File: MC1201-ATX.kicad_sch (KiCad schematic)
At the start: 248 parts, among them J1 PLD-16, J2 PLD-16, J3 PLD-16, J4 ATX-20, J5 Conn_01x01_Pin, J6 Conn_01x01_Pin, J7 Conn_01x09_Pin, P1 Conn_01x01_Pin, P10 Conn_01x01_Pin, P11 Conn_01x01_Pin, P12 Conn_01x01_Pin, P13 Conn_01x01_Pin, P14 Conn_01x01_Pin, P15 Conn_01x01_Pin, P16 Conn_01x01_Pin, P17 Conn_01x01_Pin, P18 Conn_01x01_Pin, P2 Conn_01x01_Pin, P3 Conn_01x01_Pin, P4 Conn_01x01_Pin, P5 Conn_01x01_Pin, P6 Conn_01x01_Pin, P7 Conn_01x01_Pin, P8 Conn_01x01_Pin, P9 Conn_01x01_Pin, Q1 BC547, X2 AFPC, X3 QBUS_DWK_64Pin_MBT

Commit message: Some notes, proper signal names
/MMIO renamed to /HIGHMEM, added some more net names for future references
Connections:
- net CPU_DIN: now reaches DD10.10, DD10.9, DD11.1 (CA), DD12.1 (CA), DD13.1 (CA), DD14.1 (CA), DD19.1, DD6.11, DD6.2, R3.1
- net LOCK: now reaches DD5.5, DD9.9
- net ~{MMIO} renamed ~{HIGHMEM}
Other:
- note added: "ERRATUM E0005 Сигнал LOCK не реализован."
- note removed: "ERRATUM E0005 Не подключенные входы."
- moved on the sheet: E10_5, E11_1
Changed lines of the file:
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@@
 		)
 	)
-	(text "ERRATUM E0005\nНе подключенные входы."
+	(text "ERRATUM E0005\nСигнал LOCK не реализован."
 		(exclude_from_sim no)
-		(at 154.178 238.506 0)
+		(at 149.098 237.744 0)
 		(effects
 			(font
@@
 	)
 	(junction
+		(at 568.96 207.01)
+		(diameter 0)
+		(color 0 0 0 0)
+	)
+	(junction
 		(at 29.21 398.78)
 		(diameter 0)
@@
 	)
 	(junction
-		(at 566.42 207.01)
-		(diameter 0)
-		(color 0 0 0 0)
-	)
-	(junction
 		(at 320.1029 182.88)
 		(diameter 0)
@@
 	)
 	(junction
+		(at 163.83 241.3)
+		(diameter 0)
+		(color 0 0 0 0)
+	)
+	(junction
 		(at 194.31 59.69)
 		(diameter 0)
@@
 	)
 	(junction
-		(at 568.96 196.85)
-		(diameter 0)
-		(color 0 0 0 0)
-	)
-	(junction
 		(at 146.05 156.21)
 		(diameter 0)
@@
 	)
 	(junction
-		(at 566.42 125.73)
-		(diameter 0)
-		(color 0 0 0 0)
-	)
-	(junction
 		(at 528.32 224.79)
 		(diameter 0)
@@
 	)
 	(junction
+		(at 572.77 196.85)
+		(diameter 0)
+		(color 0 0 0 0)
+	)
+	(junction
 		(at 382.27 41.91)
 		(diameter 0)
@@
 	)
 	(junction
+		(at 568.96 125.73)
+		(diameter 0)
+		(color 0 0 0 0)
+	)
+	(junction
 		(at 314.96 383.54)
 		(diameter 0)
@@
 	(wire
 		(pts
+			(xy 568.96 123.19) (xy 568.96 125.73)
+		)
+		(stroke
+			(width 0)
+			(type default)
+		)
+	)
+	(wire
+		(pts
 			(xy 283.21 109.22) (xy 288.29 109.22)
 		)
@@
 	(wire
 		(pts
+			(xy 161.29 241.3) (xy 163.83 241.3)
+		)
+		(stroke
+			(width 0)
+			(type default)
+			(color 255 0 0 1)
+		)
+	)
+	(wire
+		(pts
 			(xy 283.21 39.37) (xy 288.29 39.37)
 		)
@@
 	(wire
 		(pts
+			(xy 558.8 125.73) (xy 568.96 125.73)
+		)
+		(stroke
+			(width 0)
+			(type default)
+		)
+	)
+	(wire
+		(pts
 			(xy 481.33 347.98) (xy 499.11 347.98)
 		)
@@
 	(wire
 		(pts
-			(xy 430.53 247.65) (xy 568.96 247.65)
+			(xy 430.53 247.65) (xy 572.77 247.65)
 		)
 		(stroke
@@
 	(wire
 		(pts
-			(xy 368.3 245.11) (xy 566.42 245.11)
+			(xy 368.3 245.11) (xy 568.96 245.11)
 		)
 		(stroke
@@
 	(wire
 		(pts
-			(xy 566.42 125.73) (xy 558.8 125.73)
-		)
-		(stroke
-			(width 0)
-			(type default)
-		)
-	)
-	(wire
-		(pts
-			(xy 541.02 207.01) (xy 566.42 207.01)
+			(xy 541.02 207.01) (xy 568.96 207.01)
 		)
 		(stroke
@@
 	(wire
 		(pts
-			(xy 566.42 245.11) (xy 566.42 207.01)
+			(xy 568.96 245.11) (xy 568.96 207.01)
 		)
 		(stroke
@@
 	(wire
 		(pts
-			(xy 568.96 196.85) (xy 541.02 196.85)
+			(xy 541.02 196.85) (xy 572.77 196.85)
 		)
 		(stroke
@@
 	(wire
 		(pts
-			(xy 568.96 247.65) (xy 568.96 196.85)
+			(xy 572.77 247.65) (xy 572.77 196.85)
 		)
 		(stroke
@@
 	(wire
 		(pts
-			(xy 566.42 207.01) (xy 566.42 125.73)
+			(xy 568.96 207.01) (xy 568.96 125.73)
 		)
 		(stroke
@@
 		)
 	)
+	(label "CPU_DIN"
+		(at 392.43 228.6 0)
+		(effects
+			(font
+				(size 1.27 1.27)
+			)
+			(justify left bottom)
+		)
+	)
 	(label "~{AD15}"
 		(at 377.19 208.28 0)
@@
 		)
 	)
-	(label "~{MMIO}"
-		(at 560.07 125.73 0)
+	(label "~{HIGHMEM}"
+		(at 558.8 125.73 0)
 		(effects
 			(font
@@
 		)
 	)
+	(global_label "LOCK"
+		(shape input)
+		(at 161.29 241.3 180)
+		(fields_autoplaced yes)
+		(effects
+			(font
+				(size 1.27 1.27)
+			)
+			(justify right)
+		)
+		(property "Intersheetrefs" "${INTERSHEET_REFS}"
+			(at 153.4062 241.3 0)
+			(hide yes)
+			(show_name no)
+			(do_not_autoplace no)
+			(effects
+				(font
+					(size 1.27 1.27)
+				)
+				(justify right)
+			)
+		)
+	)
 	(global_label "~{IRQ3}"
 		(shape input)
@@
 	(symbol
 		(lib_id "Device:R")
-		(at 568.96 193.04 0)
+		(at 572.77 193.04 0)
 		(unit 1)
 		(body_style 1)
@@
 		(dnp no)
 		(property "Reference" "E10_5"
-			(at 569.214 196.85 0)
+			(at 573.024 196.85 0)
 			(show_name no)
 			(do_not_autoplace no)
@@
 		)
 		(property "Value" "2.2K"
-			(at 569.468 198.882 0)
+			(at 573.278 198.882 0)
 			(show_name no)
 			(do_not_autoplace no)
@@
 		)
 		(property "Footprint" "Resistor_THT:R_Axial_DIN0204_L3.6mm_D1.6mm_P7.62mm_Horizontal"
-			(at 567.182 193.04 90)
+			(at 570.992 193.04 90)
 			(hide yes)
 			(show_name no)
@@
 		)
 		(property "Datasheet" ""
-			(at 568.96 193.04 0)
+			(at 572.77 193.04 0)
 			(hide yes)
 			(show_name no)
@@
 		)
 		(property "Description" "Resistor"
-			(at 568.96 193.04 0)
+			(at 572.77 193.04 0)
 			(hide yes)
 			(show_name no)
@@
 	(symbol
 		(lib_id "Device:R")
-		(at 566.42 121.92 0)
+		(at 568.96 119.38 0)
 		(unit 1)
 		(body_style 1)
@@
 		(fields_autoplaced yes)
 		(property "Reference" "E11_1"
-			(at 568.96 120.6499 0)
+			(at 571.5 118.1099 0)
 			(show_name no)
 			(do_not_autoplace no)
@@
 		)
 		(property "Value" "2.2K"
-			(at 568.96 123.1899 0)
+			(at 571.5 120.6499 0)
 			(show_name no)
 			(do_not_autoplace no)
@@
 		)
 		(property "Footprint" "Resistor_THT:R_Axial_DIN0204_L3.6mm_D1.6mm_P7.62mm_Horizontal"
-			(at 564.642 121.92 90)
+			(at 567.182 119.38 90)
 			(hide yes)
 			(show_name no)
@@
 		)
 		(property "Datasheet" ""
-			(at 566.42 121.92 0)
+			(at 568.96 119.38 0)
 			(hide yes)
 			(show_name no)
@@
 		)
 		(property "Description" "Resistor"
-			(at 566.42 121.92 0)
+			(at 568.96 119.38 0)
 			(hide yes)
 			(show_name no)
@@
 	(symbol
 		(lib_id "power:VCC")
-		(at 568.96 189.23 0)
+		(at 572.77 189.23 0)
 		(unit 1)
 		(body_style 1)
@@
 		(fields_autoplaced yes)
 		(property "Reference" "#PWR066"
-			(at 568.96 193.04 0)
+			(at 572.77 193.04 0)
 			(hide yes)
 			(show_name no)
@@
 		)
 		(property "Value" "VCC"
-			(at 568.96 184.15 0)
+			(at 572.77 184.15 0)
 			(show_name no)
 			(do_not_autoplace no)
@@
 		)
 		(property "Footprint" ""
-			(at 568.96 189.23 0)
+			(at 572.77 189.23 0)
 			(hide yes)
 			(show_name no)
@@
 		)
 		(property "Datasheet" ""
-			(at 568.96 189.23 0)
+			(at 572.77 189.23 0)
 			(hide yes)
 			(show_name no)
@@
 		)
 		(property "Description" "Power symbol creates a global label with name \"VCC\""
-			(at 568.96 189.23 0)
+			(at 572.77 189.23 0)
 			(hide yes)
 			(show_name no)
@@
 	(symbol
 		(lib_id "power:VCC")
-		(at 566.42 118.11 0)
+		(at 568.96 115.57 0)
 		(unit 1)
 		(body_style 1)
@@
 		(fields_autoplaced yes)
 		(property "Reference" "#PWR065"
-			(at 566.42 121.92 0)
+			(at 568.96 119.38 0)
 			(hide yes)
 			(show_name no)
@@
 		)
 		(property "Value" "VCC"
-			(at 566.42 113.03 0)
+			(at 568.96 110.49 0)
 			(show_name no)
 			(do_not_autoplace no)
@@
 		)
 		(property "Footprint" ""
-			(at 566.42 118.11 0)
+			(at 568.96 115.57 0)
 			(hide yes)
 			(show_name no)
@@
 		)
 		(property "Datasheet" ""
-			(at 566.42 118.11 0)
+			(at 568.96 115.57 0)
 			(hide yes)
 			(show_name no)
@@
 		)
 		(property "Description" "Power symbol creates a global label with name \"VCC\""
-			(at 566.42 118.11 0)
+			(at 568.96 115.57 0)
 			(hide yes)
 			(show_name no)

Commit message: Document RAM configuration
Found out jumper settings
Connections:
- net ~{A10}: now also DX5.11 (S0); no longer DX5.10 (S1)
- net ~{A11}: now also DX5.10 (S1); no longer DX5.9 (S2)
- net ~{A12}: now also DX5.9 (S2); no longer DX6.11 (S0)
- net ~{A13}: now also DX6.11 (S0); no longer DX6.10 (S1)
- net ~{A14}: now also DX6.10 (S1); no longer DX6.9 (S2)
- net ~{A15}: now also DX6.9 (S2)
- net ~{A9}: no longer DX5.11 (S0)
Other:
- note added: "Выбор окон RAM. Информацию по установке перемычек см в документации."
- note removed: "Выбор окон RAM"
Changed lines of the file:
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@@
 		)
 	)
-	(text "Выбор окон RAM"
+	(text "Выбор окон RAM.\nИнформацию по установке\nперемычек см в документации."
 		(exclude_from_sim no)
-		(at 207.264 146.05 0)
+		(at 198.882 147.32 0)
 		(effects
 			(font
 				(size 1.27 1.27)
 			)
+			(justify left)
 		)
 	)
@@
 		)
 	)
-	(label "~{A11}"
+	(label "~{A12}"
 		(at 240.03 203.2 0)
 		(effects
@@
 		)
 	)
-	(label "~{A14}"
+	(label "~{A15}"
 		(at 284.48 205.74 0)
 		(effects
@@
 		)
 	)
-	(label "~{A9}"
+	(label "~{A10}"
 		(at 240.03 198.12 0)
 		(effects
@@
 		)
 	)
-	(label "~{A12}"
+	(label "~{A13}"
 		(at 284.48 200.66 0)
 		(effects
@@
 		)
 	)
-	(label "~{A13}"
+	(label "~{A14}"
 		(at 284.48 203.2 0)
 		(effects
@@
 		)
 	)
-	(label "~{A10}"
+	(label "~{A11}"
 		(at 240.03 200.66 0)
 		(effects

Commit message: Corrected RAM mapping
Proper config jumper settings and one more erratum.
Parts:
- EX1_8, RX7, RX8, SEL-1X2: now not fitted
- RX6: now fitted
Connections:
- net ~{SYSMEM}: now reaches DX5.4 (I0), EX1_8.2, J1.2 (Pin_2)
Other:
- note added: "ERRATUM E0008 Не декодируется окно системного ОЗУ 177600_{8}..177677_{8}"
- note added: "Задание правила выборки ОЗУ. На схеме показана конфигурация для МС1201.01."
- note removed: "Задание правила выборки ОЗУ"
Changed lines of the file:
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@@
 		)
 	)
+	(text "ERRATUM E0008\nНе декодируется окно системного\nОЗУ 177600_{8}..177677_{8}"
+		(exclude_from_sim no)
+		(at 243.84 155.194 0)
+		(effects
+			(font
+				(size 1.27 1.27)
+				(color 255 0 0 1)
+			)
+			(justify left)
+		)
+	)
 	(text "ERRATUM E0006\nЛишний резистор"
 		(exclude_from_sim no)
@@
 		)
 	)
-	(text "Задание правила\nвыборки ОЗУ"
+	(text "Задание правила\nвыборки ОЗУ. На схеме\nпоказана конфигурация\nдля МС1201.01."
 		(exclude_from_sim no)
-		(at 213.106 200.914 0)
+		(at 212.598 199.39 0)
 		(effects
 			(font
@@
 	)
 	(junction
+		(at 242.57 175.26)
+		(diameter 0)
+		(color 0 0 0 0)
+	)
+	(junction
 		(at 562.61 43.18)
 		(diameter 0)
@@
 	(wire
 		(pts
+			(xy 242.57 175.26) (xy 243.84 175.26)
+		)
+		(stroke
+			(width 0)
+			(type default)
+		)
+	)
+	(wire
+		(pts
 			(xy 523.24 173.99) (xy 528.32 173.99)
 		)
@@
 	(wire
 		(pts
+			(xy 242.57 160.02) (xy 242.57 175.26)
+		)
+		(stroke
+			(width 0)
+			(type default)
+			(color 255 0 0 1)
+		)
+	)
+	(wire
+		(pts
 			(xy 439.42 290.83) (xy 439.42 299.72)
 		)
@@
 	(wire
 		(pts
-			(xy 240.03 175.26) (xy 243.84 175.26)
+			(xy 240.03 175.26) (xy 242.57 175.26)
 		)
 		(stroke
@@
 	(wire
 		(pts
+			(xy 243.84 160.02) (xy 242.57 160.02)
+		)
+		(stroke
+			(width 0)
+			(type default)
+			(color 255 0 0 1)
+		)
+	)
+	(wire
+		(pts
 			(xy 562.61 68.58) (xy 560.07 68.58)
 		)
@@
 		)
 	)
+	(global_label "~{SYSMEM}"
+		(shape input)
+		(at 243.84 160.02 0)
+		(fields_autoplaced yes)
+		(effects
+			(font
+				(size 1.27 1.27)
+			)
+			(justify left)
+		)
+		(property "Intersheetrefs" "${INTERSHEET_REFS}"
+			(at 254.3846 160.02 0)
+			(hide yes)
+			(show_name no)
+			(do_not_autoplace no)
+			(effects
+				(font
+					(size 1.27 1.27)
+				)
+				(justify left)
+			)
+		)
+	)
 	(global_label "~{SACK}"
 		(shape input)
@@
 		(on_board yes)
 		(in_pos_files yes)
-		(dnp no)
+		(dnp yes)
 		(property "Reference" "RX8"
 			(at 221.996 204.47 90)
@@
 		(on_board yes)
 		(in_pos_files yes)
-		(dnp no)
+		(dnp yes)
 		(property "Reference" "SEL-1X2"
 			(at 205.994 207.264 90)
@@
 		(on_board yes)
 		(in_pos_files yes)
-		(dnp no)
+		(dnp yes)
 		(property "Reference" "EX1_8"
 			(at 239.014 169.926 90)
@@
 		(in_pos_files yes)
 		(dnp no)
-		(fields_autoplaced yes)
 		(property "Reference" "#PWR047"
 			(at 256.54 168.91 0)
@@
 		)
 		(property "Value" "VCC"
-			(at 256.54 160.02 0)
+			(at 256.54 161.29 0)
 			(show_name no)
 			(do_not_autoplace no)
@@
 		(on_board yes)
 		(in_pos_files yes)
-		(dnp yes)
+		(dnp no)
 		(property "Reference" "RX6"
 			(at 220.726 211.328 0)
@@
 		(on_board yes)
 		(in_pos_files yes)
-		(dnp no)
+		(dnp yes)
 		(property "Reference" "RX7"
 			(at 232.664 210.82 0)

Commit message: Fix wrong R303 value
Should be 100K
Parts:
- R303: value 1K -> 100K
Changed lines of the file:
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@@
 			)
 		)
-		(property "Value" "1K"
+		(property "Value" "100K"
 			(at 281.94 358.1399 0)
 			(show_name no)

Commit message: Add forgotten pull-ups
Pull-ups for /SEL1, /SYNC, /DOUT. Present on the board, but i forgot to place
them on the redrawn schematic.
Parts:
- added R34, R5, R6: 2.2K, Resistor_THT:R_Axial_DIN0204_L3.6mm_D1.6mm_P7.62mm_Horizontal, symbol Device:R
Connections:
- net VCC: now also R34.2, R5.2, R6.2
- net ~{DOUT}: now also R6.1
- net ~{SEL1}: now also R34.1
- net ~{SYNC}: now also R5.1

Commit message: Fix DD16 type
We use russian type designations everywhere
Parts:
- DD16: value 74LS04 -> 555LN1
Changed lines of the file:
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@@
 			)
 		)
-		(property "Value" "74LS04"
+		(property "Value" "555LN1"
 			(at 149.86 313.6899 0)
 			(show_name no)
@@
 			)
 		)
-		(property "Value" "74LS04"
+		(property "Value" "555LN1"
 			(at 346.202 264.414 0)
 			(show_name no)
@@
 			)
 		)
-		(property "Value" "74LS04"
+		(property "Value" "555LN1"
 			(at 362.966 273.05 0)
 			(show_name no)
@@
 			)
 		)
-		(property "Value" "74LS04"
+		(property "Value" "555LN1"
 			(at 55.88 45.72 0)
 			(show_name no)
@@
 			)
 		)
-		(property "Value" "74LS04"
+		(property "Value" "555LN1"
 			(at 33.02 45.72 0)
 			(show_name no)
@@
 			)
 		)
-		(property "Value" "74LS04"
+		(property "Value" "555LN1"
 			(at 344.17 250.19 0)
 			(show_name no)
@@
 			)
 		)
-		(property "Value" "74LS04"
+		(property "Value" "555LN1"
 			(at 48.26 69.85 0)
 			(show_name no)

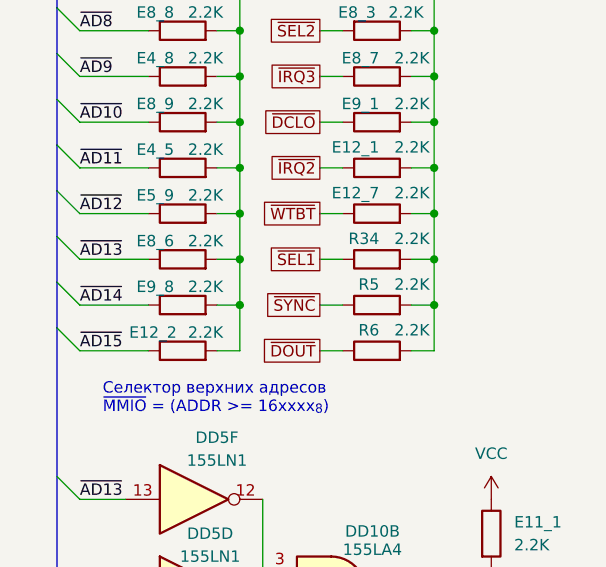
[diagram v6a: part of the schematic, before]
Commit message: Corrected pull-up values
Proper values for R5, R6, R34. According to original schematic.
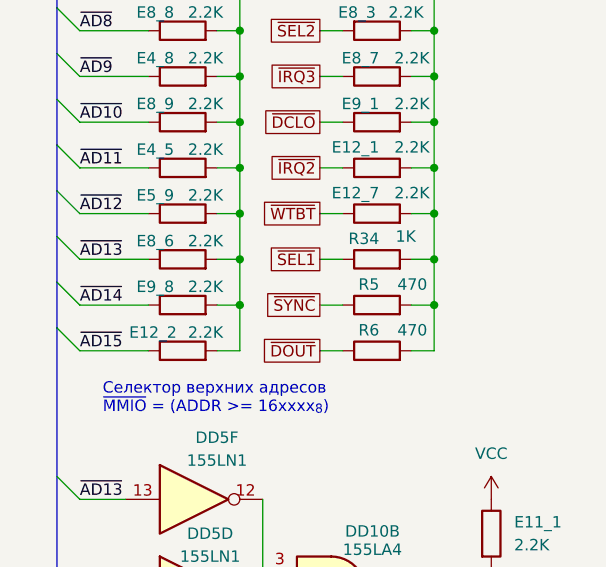
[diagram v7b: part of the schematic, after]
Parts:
- R34: value 2.2K -> 1K
- R5, R6: value 2.2K -> 470
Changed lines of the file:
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@@
 			)
 		)
-		(property "Value" "2.2K"
-			(at 562.102 96.774 90)
+		(property "Value" "470"
+			(at 561.848 96.774 90)
 			(show_name no)
 			(do_not_autoplace no)
@@
 			)
 		)
-		(property "Value" "2.2K"
-			(at 562.102 86.614 90)
+		(property "Value" "1K"
+			(at 560.578 86.36 90)
 			(show_name no)
 			(do_not_autoplace no)
@@
 			)
 		)
-		(property "Value" "2.2K"
-			(at 562.102 91.694 90)
+		(property "Value" "470"
+			(at 561.848 91.694 90)
 			(show_name no)
 			(do_not_autoplace no)

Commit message: Some updates
Proper documentation of RAM configuration and memory mapping. Found erratum
E0009.
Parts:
- J3: now not fitted
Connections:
- net ~{HIGHMEM} renamed ~{BS7}
- net ~{SYSMEM} renamed SYSMEM
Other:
- note added: "ERRATUM E0009: Вывод 8 DD36A соединён с +5В. !!! ОТСОЕДИНИТЬ !!!"
- note added: "J3: соединить пайкой 1 и 2. Разъём не устанавливать."
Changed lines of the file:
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@@
 		)
 	)
+	(text "ERRATUM E0009: Вывод 8 DD36A\nсоединён с +5В. !!! ОТСОЕДИНИТЬ !!!"
+		(exclude_from_sim no)
+		(at 397.764 253.746 0)
+		(effects
+			(font
+				(size 1.27 1.27)
+				(thickness 0.1588)
+				(color 255 0 0 1)
+			)
+		)
+	)
 	(text "ERRATUM E0008\nНе декодируется окно системного\nОЗУ 177600_{8}..177677_{8}"
 		(exclude_from_sim no)
@@
 	(text "Задание правила\nвыборки ОЗУ. На схеме\nпоказана конфигурация\nдля МС1201.01."
 		(exclude_from_sim no)
-		(at 212.598 199.39 0)
+		(at 199.39 219.71 0)
 		(effects
 			(font
@@
 		)
 	)
+	(text "J3: соединить пайкой 1 и 2.\nРазъём не устанавливать."
+		(exclude_from_sim no)
+		(at 291.084 146.558 0)
+		(effects
+			(font
+				(size 1.27 1.27)
+			)
+			(justify right)
+		)
+	)
 	(text "Элементы, помеченные\nкак \"не устанавливать\",\nиспользуются в оригинальной\nсхеме для связи с силовым\nинтерфейсом МПИ, который\nв данной схеме отсутствует\n(если не указано иное)"
 		(exclude_from_sim no)
@@
 	)
 	(junction
+		(at 251.46 132.08)
+		(diameter 0)
+		(color 0 0 0 0)
+	)
+	(junction
 		(at 382.27 132.08)
 		(diameter 0)
@@
 	)
 	(junction
-		(at 251.46 140.97)
-		(diameter 0)
-		(color 0 0 0 0)
-	)
-	(junction
 		(at 290.83 157.48)
 		(diameter 0)
@@
 	(bus
 		(pts
-			(xy 281.94 140.97) (xy 281.94 203.2)
+			(xy 281.94 149.86) (xy 281.94 203.2)
 		)
 		(stroke
@@
 	(bus
 		(pts
-			(xy 251.46 140.97) (xy 281.94 140.97)
+			(xy 251.46 149.86) (xy 281.94 149.86)
 		)
 		(stroke
@@
 		)
 	)
+	(polyline
+		(pts
+			(xy 290.83 149.86) (xy 303.53 149.86)
+		)
+		(stroke
+			(width 0.254)
+			(type solid)
+		)
+	)
 	(wire
 		(pts
@@
 		)
 	)
+	(bus
+		(pts
+			(xy 251.46 132.08) (xy 251.46 149.86)
+		)
+		(stroke
+			(width 0)
+			(type default)
+		)
+	)
 	(wire
 		(pts
@@
 	(bus
 		(pts
-			(xy 247.65 33.02) (xy 247.65 140.97)
+			(xy 247.65 33.02) (xy 247.65 132.08)
 		)
 		(stroke
@@
 	(bus
 		(pts
-			(xy 247.65 140.97) (xy 251.46 140.97)
+			(xy 247.65 132.08) (xy 251.46 132.08)
 		)
 		(stroke
@@
 	(bus
 		(pts
-			(xy 251.46 33.02) (xy 251.46 140.97)
+			(xy 251.46 33.02) (xy 251.46 132.08)
 		)
 		(stroke
@@
 		)
 	)
+	(label "~{BS7}"
+		(at 554.99 207.01 0)
+		(effects
+			(font
+				(size 1.27 1.27)
+			)
+			(justify left bottom)
+		)
+	)
 	(label "~{A3}"
 		(at 254 99.06 0)
@@
 		)
 	)
-	(label "~{HIGHMEM}"
-		(at 558.8 125.73 0)
-		(effects
-			(font
-				(size 1.27 1.27)
-			)
-			(justify left bottom)
-		)
-	)
 	(label "~{AD0}"
 		(at 283.21 36.83 0)
@@
 		)
 	)
-	(global_label "~{SYSMEM}"
+	(global_label "SYSMEM"
 		(shape input)
 		(at 243.84 160.02 0)
@@
 		(on_board yes)
 		(in_pos_files yes)
-		(dnp no)
+		(dnp yes)
 		(property "Reference" "J3"
 			(at 297.18 144.78 0)
